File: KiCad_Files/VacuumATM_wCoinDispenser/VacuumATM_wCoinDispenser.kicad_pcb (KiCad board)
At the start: 2 copper layers, 72.5 x 70 mm, 10 parts, among them J1 VacButton, J2 Neopixel, J3 9g Servo, J4 User2_Button, J5 User1_Button

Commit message: Updates to KiCAD, images
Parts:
- added Reset: ResetButton, TerminalBlock_Phoenix:TerminalBlock_Phoenix_MKDS-1,5-2_1x02_P5.00mm_Horizontal, F.Cu at (154.0, 84.5)
- 9g Servo: renamed from J3
- CamSwitch: renamed from J1; value VacButton -> CamButton
- User 2 Button: renamed from J4
- User1 Button: renamed from J5
- moved 9g Servo 11.4 mm to (154.0, 121.0)
- moved NeoPixel 11.3 mm to (154.0, 101.7)
- renumbered J2 to NeoPixel
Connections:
- A1 pad 1: unconnected-(A1-~{RESET}-Pad1) -> Net-(A1-~{RESET})
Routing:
- net Net-(A1-~{RESET}): track 0.00 -> 44.1 mm
- net GND: track 70.2 -> 88.1 mm
- net Net-(A1-D2): track 24.3 -> 16.6 mm
- net VBUS: track 40.0 -> 34.7 mm
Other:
- board text added: "3.3V"
- board text added: "5V"
- board text added: "GND"
- board text added: "Photon 2"
- board text added: "Signal"

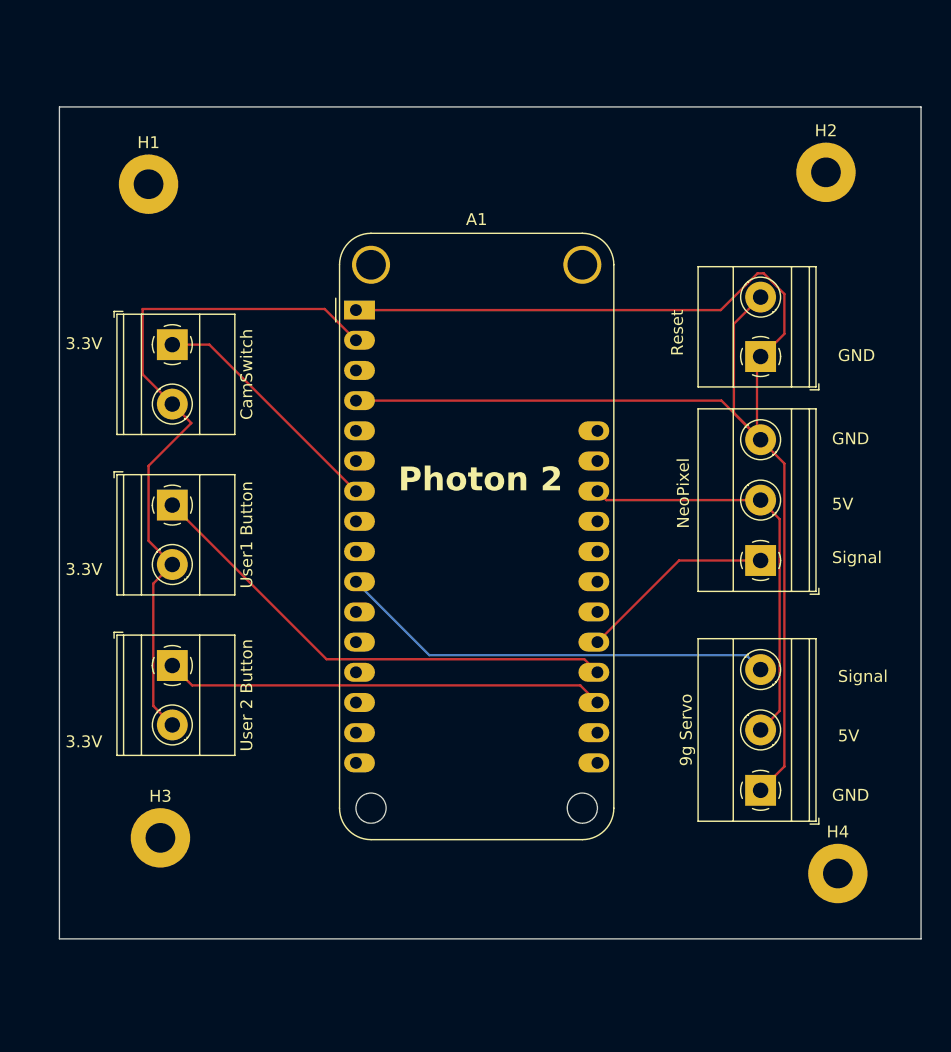
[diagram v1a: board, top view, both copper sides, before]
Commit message: Redesigned PCB, made Gerber files
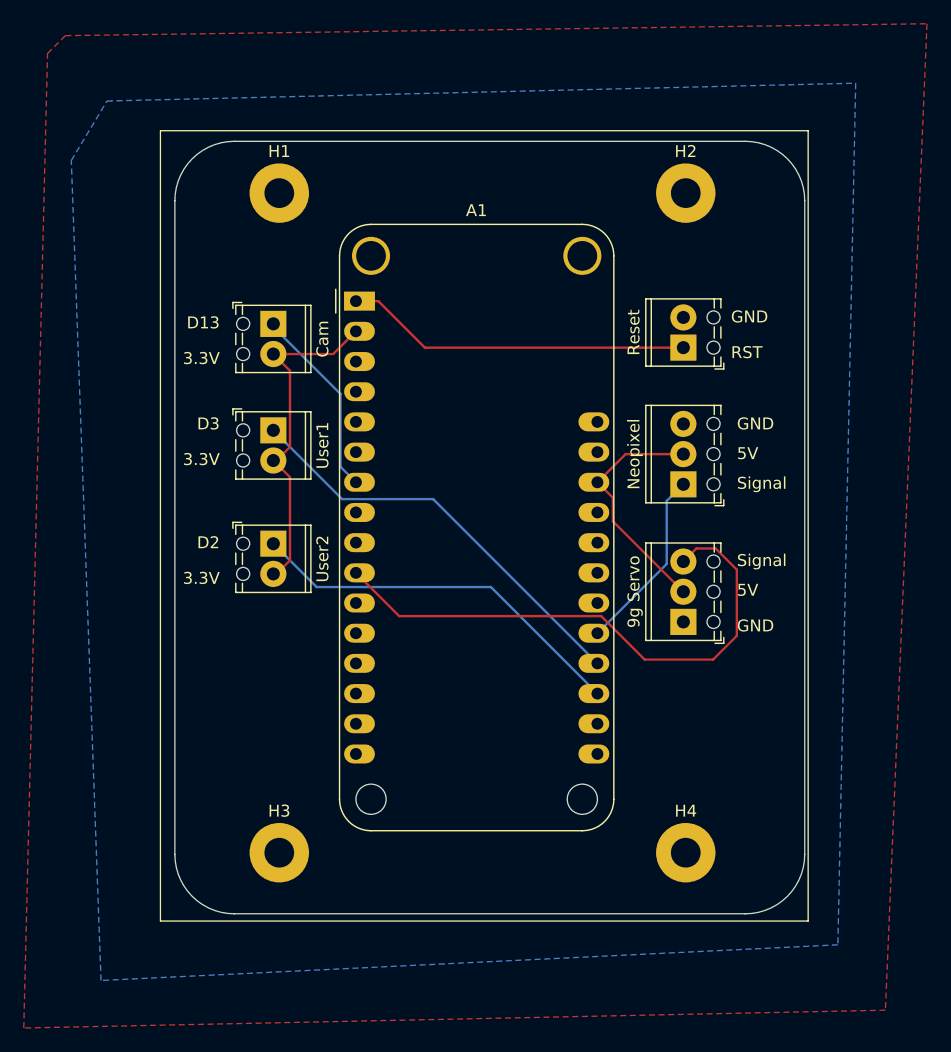
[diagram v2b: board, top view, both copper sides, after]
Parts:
- 9g Servo: footprint TerminalBlock_Phoenix:TerminalBlock_Phoenix_MKDS-1,5-3-5.08_1x03_P5.08mm_Horizontal -> TerminalBlock_Phoenix:TerminalBlock_Phoenix_MPT-0,5-3-2.54_1x03_P2.54mm_Horizontal
- Cam: renamed from CamSwitch; footprint TerminalBlock_Phoenix:TerminalBlock_Phoenix_MKDS-1,5-2_1x02_P5.00mm_Horizontal -> TerminalBlock_Phoenix:TerminalBlock_Phoenix_MPT-0,5-2-2.54_1x02_P2.54mm_Horizontal
- Neopixel: renamed from NeoPixel; footprint TerminalBlock_Phoenix:TerminalBlock_Phoenix_MKDS-1,5-3-5.08_1x03_P5.08mm_Horizontal -> TerminalBlock_Phoenix:TerminalBlock_Phoenix_MPT-0,5-3-2.54_1x03_P2.54mm_Horizontal
- Reset: footprint TerminalBlock_Phoenix:TerminalBlock_Phoenix_MKDS-1,5-2_1x02_P5.00mm_Horizontal -> TerminalBlock_Phoenix:TerminalBlock_Phoenix_MPT-0,5-2-2.54_1x02_P2.54mm_Horizontal
- User1: renamed from User1 Button; footprint TerminalBlock_Phoenix:TerminalBlock_Phoenix_MKDS-1,5-2_1x02_P5.00mm_Horizontal -> TerminalBlock_Phoenix:TerminalBlock_Phoenix_MPT-0,5-2-2.54_1x02_P2.54mm_Horizontal
- User2: renamed from User 2 Button; footprint TerminalBlock_Phoenix:TerminalBlock_Phoenix_MKDS-1,5-2_1x02_P5.00mm_Horizontal -> TerminalBlock_Phoenix:TerminalBlock_Phoenix_MPT-0,5-2-2.54_1x02_P2.54mm_Horizontal
- moved 9g Servo 15.6 mm to (147.5, 106.8)
- moved User2 13.3 mm to (113.0, 100.2)
- moved H4 12.9 mm to (147.7, 126.2)
- moved H2 11.9 mm to (147.7, 70.8)
- moved H1 11.0 mm to (113.5, 70.8)
- moved User1 10.6 mm to (113.0, 90.7)
- moved H3 10.1 mm to (113.5, 126.2)
- moved Neopixel 9.13 mm to (147.5, 95.2)
- moved Cam 8.68 mm to (113.0, 81.8)
- moved Reset 6.54 mm to (147.5, 83.8)
- moved A1 0.75 mm to (120.0, 79.8)
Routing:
- net GND: track 88.1 -> 0.00 mm
- net +3.3V: track 59.4 -> 28.9 mm
- net Net-(A1-~{RESET}): track 44.1 -> 29.2 mm
- net VBUS: track 34.7 -> 20.4 mm
- net Net-(A1-A5): track 37.1 -> 47.2 mm
- net Net-(A1-D1): track 41.6 -> 35.4 mm
- net Net-(A1-D0): track 37.1 -> 32.5 mm
- net Net-(A1-A2): track 20.6 -> 16.2 mm
- net Net-(A1-D2): track 16.6 -> 15.5 mm
- added copper zone on B.Cu, net (none)
- added copper zone on F.Cu, net GND
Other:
- board size 72.5 x 70 mm -> 53 x 65 mm
- board text added: "D13"
- board text added: "D2"
- board text added: "D3"
- board text added: "Daniel Stromberg 2024"
- board text added: "RST"
- board text added: "Vacuum ATM"

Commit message: Updated KiCAD files
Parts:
- A1: value Adafruit_Feather_Generic -> Photon2; footprint Module:Adafruit_Feather_WithMountingHoles -> Particle:Photon2
- J3: renamed from 9g Servo
- renumbered Cam to J1, Neopixel to J2, User2 to J4, User1 to J5, Reset to J6
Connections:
- A1 pad 19: Net-(A1-D0) -> Net-(A1-D2)
- A1 pad 21: Net-(A1-D2) -> Net-(A1-D4)
- J4 pad 1: Net-(A1-D0) -> Net-(A1-D4)
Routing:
- net Net-(A1-D4): track 0.00 -> 35.0 mm
- net Net-(A1-D0): track 32.5 -> 0.00 mm
- net Net-(A1-D2): track 15.5 -> 20.6 mm
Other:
- board text added: "D4"
- board text removed: "D2"
